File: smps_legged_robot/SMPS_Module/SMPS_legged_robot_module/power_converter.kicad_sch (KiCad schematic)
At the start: 80 parts, among them IC1 LTC3889EUKG#PBF, IC2 LTC3889EUKG#PBF, Q1 NMOS, Q10 NMOS, Q2 NMOS, Q3 NMOS, Q4 NMOS, Q5 PNP, Q6 PNP, Q7 NMOS, Q8 NMOS, Q9 NMOS

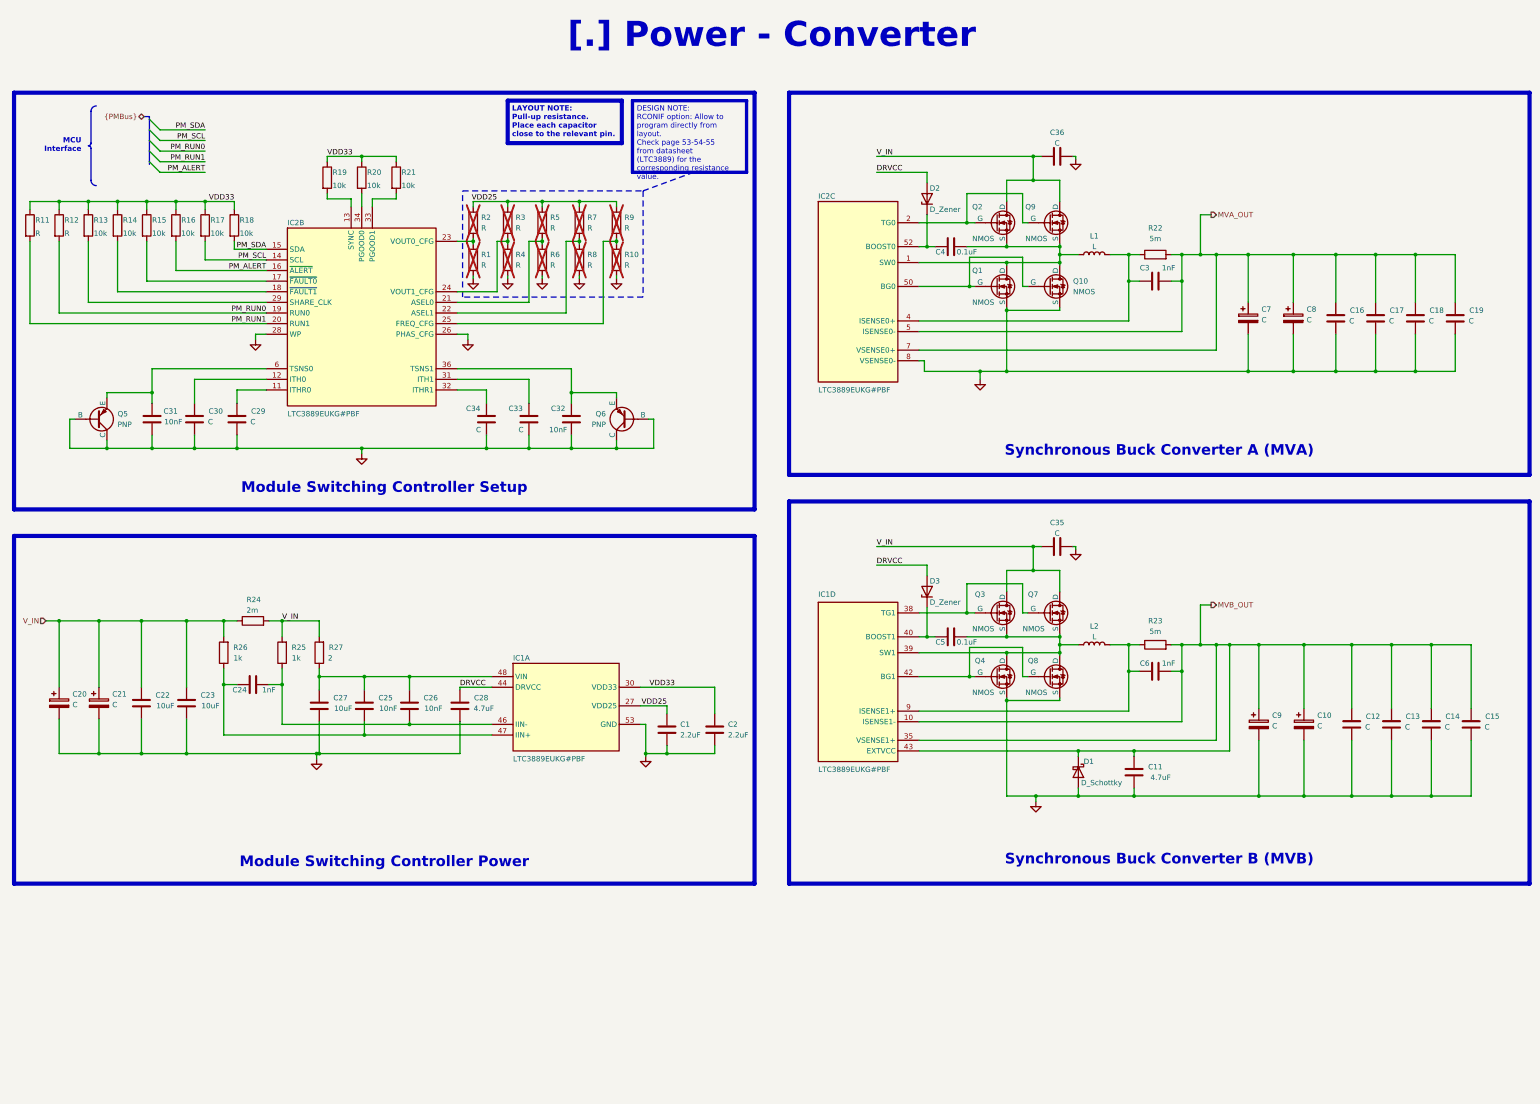
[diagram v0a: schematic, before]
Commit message: Buck module finished pending review
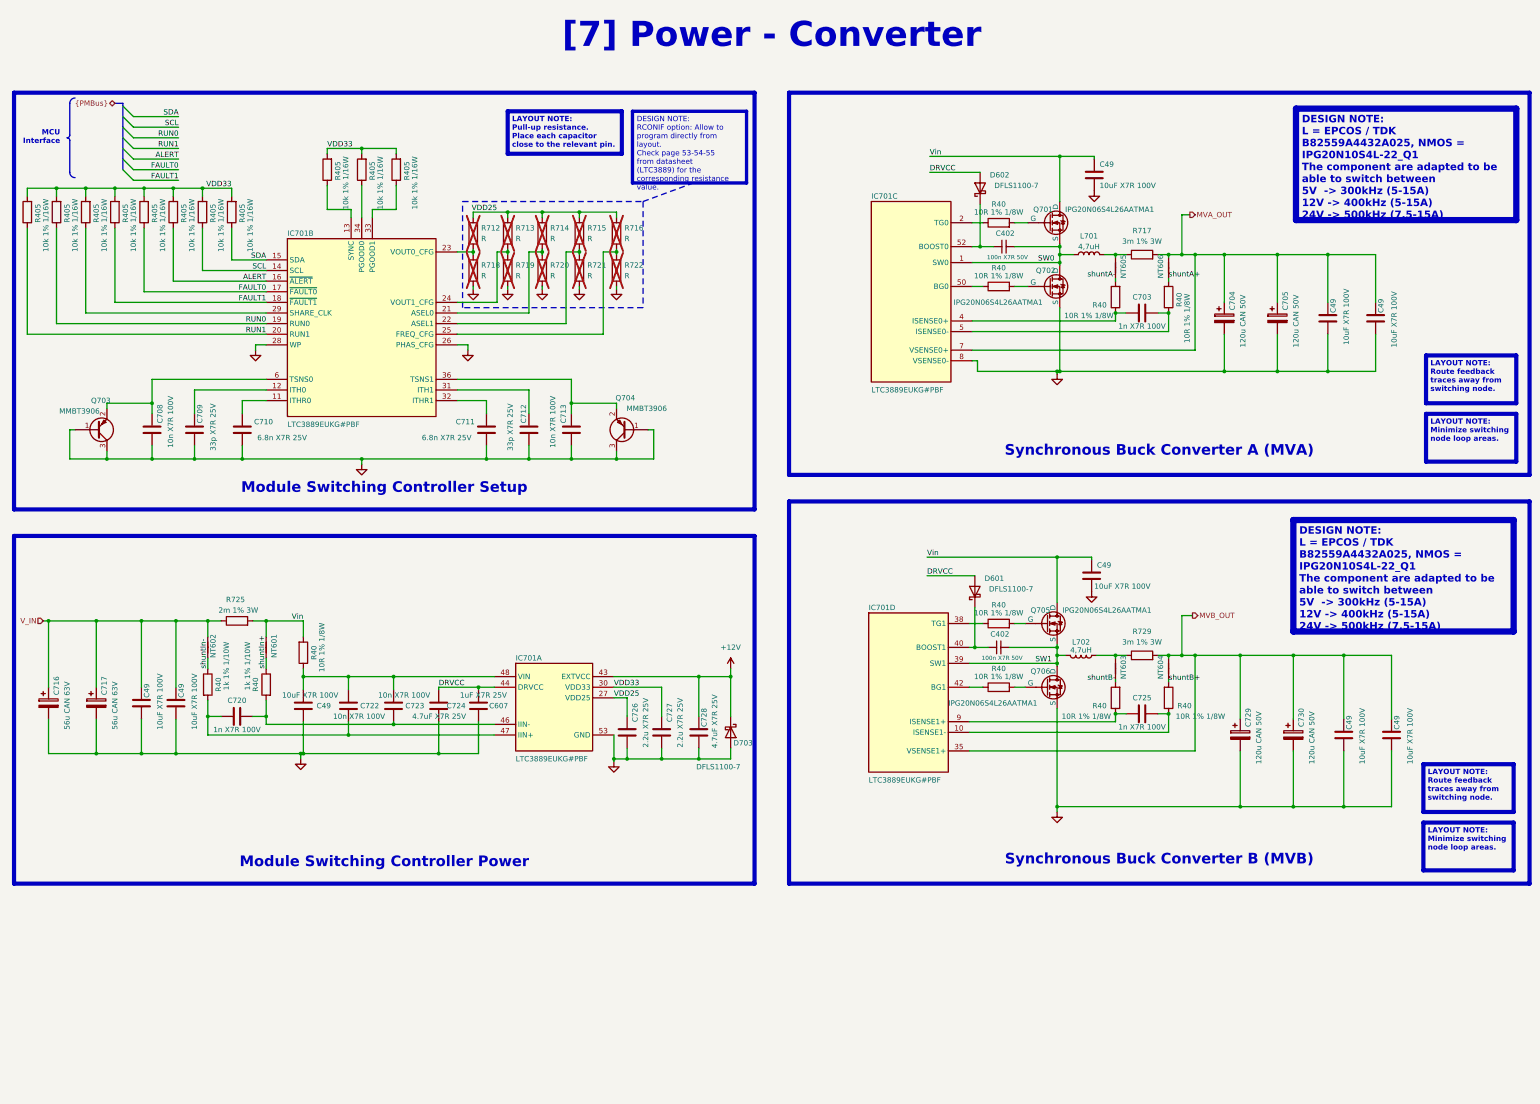
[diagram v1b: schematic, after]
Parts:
- removed C1, C2: 2.2uF, symbol Device:C
- removed C10, C21, C7, C8, C9: C, symbol Device:C_Polarized
- removed C11, C28: 4.7uF, symbol Device:C
- removed C12, C13, C14, C15, C16, C17, C18, C19, C30, C33, C34, C35, C36: C, symbol Device:C
- removed C22, C23, C27: 10uF, symbol Device:C
- removed C24, C3: 1nF, symbol Device:C
- removed C31, C32: 10nF, symbol Device:C
- removed C4, C5: 0.1uF, symbol Device:C
- removed D1: D_Schottky, symbol Device:D_Schottky
- removed D2, D3: D_Zener, symbol Device:D_Zener
- removed Q10, Q2, Q7, Q8, Q9: NMOS, symbol Simulation_SPICE:NMOS
- removed Q5, Q6: PNP, symbol Simulation_SPICE:PNP
- removed R11, R12: R, symbol Device:R
- removed R13, R14, R15, R16, R17, R18, R19, R20, R21: 10k, symbol Device:R
- removed R23: 5m, symbol Device:R
- removed R24: 2m, symbol Device:R
- removed R25, R26: 1k, symbol Device:R
- removed R27: 2, symbol Device:R
- added C402 (x2): 100n X7R 50V, 0_capacitor_smd:C_0402_1005_DensityHigh, symbol Device:C_Small
- added C49 (x9): 10uF X7R 100V, 0_capacitor_smd:C_1210_3225_DensityHigh, symbol Device:C
- added C607: 1uF X7R 25V, 0_capacitor_smd:C_0603_1608_DensityHigh, symbol Device:C
- added C703, C720: 1n X7R 100V, 0_capacitor_smd:C_0402_1005_DensityHigh, symbol Device:C
- added C704, C705, C729, C730: 120u CAN 50V, 0_capacitor_smd:Hybrid_G_VP, symbol Device:C_Polarized
- added C708, C713: 10n X7R 100V, 0_capacitor_smd:C_0402_1005_DensityHigh, symbol Device:C
- added C709, C712: 33p X7R 25V, 0_capacitor_smd:C_0402_1005_DensityHigh, symbol Device:C
- added C711: 6.8n X7R 25V, 0_capacitor_smd:C_0402_1005_DensityHigh, symbol Device:C
- added C717: 56u CAN 63V, 0_capacitor_smd:Hybrid_G_VP, symbol Device:C_Polarized
- added C724, C728: 4.7uF X7R 25V, 0_capacitor_smd:C_1210_3225_DensityHigh, symbol Device:C
- added C726, C727: 2.2u X7R 25V, 0_capacitor_smd:C_0805_2012_DensityHigh, symbol Device:C
- added D601, D602, D703: DFLS1100-7, 0_diode_smd:Diodes_Inc.-PowerDI123-03_2017-0-MFG, symbol Device:D_Schottky
- added NT601, NT602, NT603, NT604, NT605, NT606: NetTie_2, 0_net_tie:NetTie-2_SMD_Pad0.2mm, symbol Device:NetTie_2
- added Q701: IPG20N06S4L26AATMA1, 0_transistor_fet:Infineon-IPG20N06S4L-26A-Manufacturer_Recommended, symbol Simulation_SPICE:NMOS
- added Q703, Q704: MMBT3906, Package_TO_SOT_SMD:SOT-23, symbol Transistor_BJT:MMBT3906
- added R40 (x2): 1k 1% 1/10W, 0_resistor_smd:R_0603_1608_DensityHigh, symbol Device:R
- added R40 (x9): 10R 1% 1/8W, 0_resistor_smd:R_0402_1005_DensityHigh, symbol Device:R
- added R405 (x11): 10k 1% 1/16W, 0_resistor_smd:R_0402_1005_DensityHigh, symbol Device:R
- added R725: 2m 1% 3W, Resistor_SMD:R_2512_6332Metric_Pad1.40x3.35mm_HandSolder, symbol Device:R
- added R729: 3m 1% 3W, 0_resistor_smd:RESC6432X135N, symbol Device:R
- C710: renamed from C29; value C -> 6.8n X7R 25V; footprint (none) -> 0_capacitor_smd:C_0402_1005_DensityHigh
- C716: renamed from C20; value C -> 56u CAN 63V; footprint (none) -> 0_capacitor_smd:Hybrid_G_VP
- C722: renamed from C25; value 10nF -> 10n X7R 100V; footprint (none) -> 0_capacitor_smd:C_0402_1005_DensityHigh
- C723: renamed from C26; value 10nF -> 10n X7R 100V; footprint (none) -> 0_capacitor_smd:C_0402_1005_DensityHigh
- C725: renamed from C6; value 1nF -> 1n X7R 100V; footprint (none) -> 0_capacitor_smd:C_0402_1005_DensityHigh
- IC701: renamed from IC1; footprint QFN50P700X800X80-53N-D -> 0_switching_regulator:QFN50P700X800X80-53N-D
- IC701: renamed from IC2; footprint QFN50P700X800X80-53N-D -> 0_switching_regulator:QFN50P700X800X80-53N-D
- L701: renamed from L1; value L -> 4,7uH; footprint (none) -> 0_capacitor_smd:PQ2617BHA4R7K
- L702: renamed from L2; value L -> 4,7uH; footprint (none) -> 0_capacitor_smd:PQ2617BHA4R7K
- Q702: renamed from Q1; value NMOS -> IPG20N06S4L26AATMA1; footprint (none) -> 0_transistor_fet:Infineon-IPG20N06S4L-26A-Manufacturer_Recommended
- Q705: renamed from Q3; value NMOS -> IPG20N06S4L26AATMA1; footprint (none) -> 0_transistor_fet:Infineon-IPG20N06S4L-26A-Manufacturer_Recommended
- Q706: renamed from Q4; value NMOS -> IPG20N06S4L26AATMA1; footprint (none) -> 0_transistor_fet:Infineon-IPG20N06S4L-26A-Manufacturer_Recommended
- R712: renamed from R2; footprint (none) -> 0_resistor_smd:R_0402_1005_DensityHigh
- R713: renamed from R3; footprint (none) -> 0_resistor_smd:R_0402_1005_DensityHigh
- R714: renamed from R5; footprint (none) -> 0_resistor_smd:R_0402_1005_DensityHigh
- R715: renamed from R7; footprint (none) -> 0_resistor_smd:R_0402_1005_DensityHigh
- R716: renamed from R9; footprint (none) -> 0_resistor_smd:R_0402_1005_DensityHigh
- R717: renamed from R22; value 5m -> 3m 1% 3W; footprint (none) -> 0_resistor_smd:RESC6432X135N
- R718: renamed from R1; footprint (none) -> 0_resistor_smd:R_0402_1005_DensityHigh
- R719: renamed from R4; footprint (none) -> 0_resistor_smd:R_0402_1005_DensityHigh
- R720: renamed from R6; footprint (none) -> 0_resistor_smd:R_0402_1005_DensityHigh
- R721: renamed from R8; footprint (none) -> 0_resistor_smd:R_0402_1005_DensityHigh
- R722: renamed from R10; footprint (none) -> 0_resistor_smd:R_0402_1005_DensityHigh
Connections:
- net DRVCC: now also C607.2, C724.2, D601.2 (A), D602.2 (A)
- net GND: now also C49.2, C49.2, C49.2, C49.2, C49.2, C49.2, C49.2, C49.2, C49.2, C607.1, C704.2, C705.2, C708.1, C709.1, C711.1, C712.1, C713.1, C717.2, C724.1, C726.1, C727.1, C728.1, C729.2, C730.2, D703.2 (A), Q703.1 (B), Q703.3 (C), Q704.1 (B), Q704.3 (C)
- net MVA_OUT: now also C49.1, C49.1, C704.1, C705.1, NT606.1; no longer IC701.5 (ISENSE0-)
- net MVB_OUT: now also C49.1, C49.1, C729.1, C730.1, NT604.1, R729.2; no longer C725.2, IC701.10 (ISENSE1-), IC701.43 (EXTVCC)
- net VDD25: now also C726.2
- net VDD33: now also C727.2, R405.2, R405.2, R405.2, R405.2, R405.2, R405.2, R405.2, R405.2, R405.2, R405.2, R405.2
- net V_IN: now also C49.1, C49.1, C717.1, NT602.1, R725.1; no longer Q705.1 (D)
- net at Q705.2 (G): now also R40.2; no longer IC701.38 (TG1)
- net SW1: now reaches IC701.39 (SW1), Q705.3 (S), Q706.1 (D)
- net SW1: now also L702.2, C402.2; no longer L702.1
- net SW0: now reaches IC701.1 (SW0), L701.1, Q702.1 (D)
- net SW0: now also C402.2, Q701.3 (S)
- net at Q702.2 (G): now also R40.2; no longer IC701.50 (BG0)
- net at IC701.31 (ITH1): now also C712.2
- net at IC701.52 (BOOST0): now also C402.1, D602.1 (K)
- net at C722.2, C723.2, IC701.48 (VIN): now also C49.1, R40.1
- net at IC701.6 (TSNS0): now also C708.2, Q703.2 (E)
- net at L701.2, R717.1: now also NT605.1; no longer IC701.4 (ISENSE0+)
- net at C723.1, IC701.46 (IIN-): now also C720.2, R40.2
- net at C722.1, IC701.47 (IIN+): now also C720.1, R40.2
- net at IC701.13 (SYNC): now also R405.1
- net at IC701.2 (TG0): now also R40.1
- net at IC701.33 (PGOOD1): now also R405.1
- net at IC701.29 (SHARE_CLK): now also R405.1
- net FAULT0: now reaches IC701.17 (~{FAULT0})
- net FAULT0: now also R405.1
- net at IC701.12 (ITH0): now also C709.2
- net FAULT1: now reaches IC701.18 (~{FAULT1})
- net FAULT1: now also R405.1
- net at IC701.32 (ITHR1): now also C711.2
- net at IC701.34 (PGOOD0): now also R405.1
- net at IC701.36 (TSNS1): now also C713.2, Q704.2 (E)
- net at C725.1, IC701.9 (ISENSE1+): now also R40.1; no longer L702.2
- net at IC701.40 (BOOST1): now also C402.1, D601.1 (K)
- net at IC701.42 (BG1): now also R40.1; no longer Q706.2 (G)
- net PM_ALERT renamed ALERT
- net ALERT: now also R405.1
- net PM_RUN0 renamed RUN0
- net RUN0: now also R405.1
- net PM_RUN1 renamed RUN1
- net RUN1: now also R405.1
- net PM_SCL renamed SCL
- net SCL: now also R405.1
- net PM_SDA renamed SDA
- net SDA: now also R405.1
- new net: Q701.2 (G), R40.2
- new net: C703.2, IC701.5 (ISENSE0-), R40.1
- new net: C725.2, IC701.10 (ISENSE1-), R40.1
- new net: IC701.38 (TG1), R40.1
- new net: L702.1, NT603.1, R729.1
- new net: Q706.2 (G), R40.2
- new net: C703.1, IC701.4 (ISENSE0+), R40.1
- new net: IC701.50 (BG0), R40.1
- new net +12V: C728.2, D703.1 (K), IC701.43 (EXTVCC)
- new net Vin: C49.1, C49.1, NT601.1, Q701.1 (D), Q705.1 (D), R40.2, R725.2
- new net shuntA+: NT606.2, R40.2
- new net shuntA-: NT605.2, R40.2
- new net shuntB+: NT604.2, R40.2
- new net shuntB-: NT603.2, R40.2
- new net shuntIn+: NT601.2, R40.1
- new net shuntIn-: NT602.2, R40.1
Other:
- moved on the sheet: C710, C716, C722, C723, C725, IC701B, IC701C, L701, L702, Q702, Q705, Q706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

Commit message: Correction module
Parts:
- removed C49 (x3): 10uF X7R 100V, 0_capacitor_smd:C_1210_3225_DensityHigh, symbol Device:C
- removed C716, C717: 56u CAN 63V, 0_capacitor_smd:Hybrid_G_VP, symbol Device:C_Polarized
- removed C727: 2.2u X7R 25V, 0_capacitor_smd:C_0805_2012_DensityHigh, symbol Device:C
- removed C728: 4.7uF X7R 25V, 0_capacitor_smd:C_1210_3225_DensityHigh, symbol Device:C
- removed R40 (x4): 10R 1% 1/8W, 0_resistor_smd:R_0402_1005_DensityHigh, symbol Device:R
- added C716: 2.2u X7R 25V, 0_capacitor_smd:C_0603_1608_DensityHigh, symbol Device:C
- added C717: 4.7u X5R 25V, 0_capacitor_smd:C_0402_1005_DensityHigh, symbol Device:C
- added C718: 10n X7R 100V, 0_capacitor_smd:C_0402_1005_DensityHigh, symbol Device:C
- added D701, D702: LED, symbol Device:LED
- added Q707, Q708: NMOS, symbol Simulation_SPICE:NMOS
- added R40 (x6): 2R 1% 1/8W, 0_resistor_smd:R_0402_1005_DensityHigh, symbol Device:R
- added R736, R737: R, symbol Device:R
- added TP409: 3V3LTC, 0_testpoint:TestPoint_Pad_D0.5mm_Back, symbol Connector:TestPoint
- added TP409: VIN_MOS, 0_testpoint:TestPoint_Pad_D0.5mm_Front, symbol Connector:TestPoint
- added TP409: VIN, 0_testpoint:TestPoint_Pad_D0.5mm_Front, symbol Connector:TestPoint
- added TP409: DRVCC, 0_testpoint:TestPoint_Pad_D0.5mm_Back, symbol Connector:TestPoint
- added TP409: MVB_OUT, 0_testpoint:TestPoint_Pad_D0.5mm_Front, symbol Connector:TestPoint
- added TP409: SW1_L, 0_testpoint:TestPoint_Pad_D0.5mm_Front, symbol Connector:TestPoint
- added TP409: SW0, 0_testpoint:TestPoint_Pad_D0.5mm_Front, symbol Connector:TestPoint
- added TP409: SW0_L, 0_testpoint:TestPoint_Pad_D0.5mm_Front, symbol Connector:TestPoint
- added TP409: MVA_OUT, 0_testpoint:TestPoint_Pad_D0.5mm_Front, symbol Connector:TestPoint
- added TP409: 2V5LTC, 0_testpoint:TestPoint_Pad_D0.5mm_Back, symbol Connector:TestPoint
- added TP409: SW1, 0_testpoint:TestPoint_Pad_D0.5mm_Front, symbol Connector:TestPoint
- C607: value 1uF X7R 25V -> 1u X7R 25V
- C724: value 4.7uF X7R 25V -> 4.7u X5R 25V; footprint 0_capacitor_smd:C_1210_3225_DensityHigh -> 0_capacitor_smd:C_0402_1005_DensityHigh
- C726: footprint 0_capacitor_smd:C_0805_2012_DensityHigh -> 0_capacitor_smd:C_0603_1608_DensityHigh
- Q703, Q704: value MMBT3906 -> PMBT3906,215
- R40: value 10R 1% 1/8W -> 2R 1% 1/8W
- R405: value 10k 1% 1/16W -> 5k 1% 1/16W
- R712, R713, R714, R715, R718, R719, R720, R721: now left out of the parts list
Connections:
- net +12V: now also C717.2, R736.1, R737.1
- net DRVCC: now also TP409.1
- net GND: now also C716.1, C717.1, C718.1, Q707.3 (S), Q708.3 (S)
- net MVA_OUT: now also TP409.1
- net MVB_OUT: now also TP409.1
- net SW0: now also TP409.1
- net SW1: now also TP409.1
- net at Q705.2 (G): now also R40.1
- net at Q701.2 (G): now also R40.1
- net SW0_L: now reaches L701.2, NT605.1, R717.1
- net SW0_L: now also TP409.1
- net at IC701.2 (TG0): now also R40.2
- net VIN: now reaches C722.2, C723.2, IC701.48 (VIN), R40.1
- net VIN: now also C718.2, TP409.1
- net PGOOD1: now reaches IC701.33 (PGOOD1), R405.1
- net PGOOD1: now also Q708.2 (G)
- net at D601.1 (K), IC701.40 (BOOST1): now also R40.2; no longer C402.1
- net at Q702.2 (G): now also R40.1
- net at IC701.38 (TG1): now also R40.2
- net SW1_L: now reaches L702.1, NT603.1, R729.1
- net SW1_L: now also TP409.1
- net SHARE_CLK: now reaches IC701.29 (SHARE_CLK), R405.1
- net at IC701.42 (BG1): now also R40.2
- net at Q706.2 (G): now also R40.1
- net PGOOD0: now reaches IC701.34 (PGOOD0), R405.1
- net PGOOD0: now also Q707.2 (G)
- net SYNC: now reaches IC701.13 (SYNC), R405.1
- net at IC701.50 (BG0): now also R40.2
- net at D602.1 (K), IC701.52 (BOOST0): now also R40.2; no longer C402.1
- net ALERT renamed ~{ALERT}
- net FAULT0 renamed ~{FAULT0}
- net FAULT1 renamed ~{FAULT1}
- net VDD25 renamed +2V5LTC
- net +2V5LTC: now also TP409.1
- net VDD33 renamed +3.3VLTC
- net +3.3VLTC: now also C716.2, TP409.1
- net V_IN renamed +VBAT_FILTERED
- net Vin renamed VIN_MOS
- net VIN_MOS: now also TP409.1
- new net: D701.1 (K), Q707.1 (D)
- new net: D701.2 (A), R736.2
- new net: C402.1, R40.1 (x2)
- new net: D702.2 (A), R737.2
- new net: D702.1 (K), Q708.1 (D)
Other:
- moved on the sheet: C402, C49, C607, C704, C705, C708, C709, C710, C711, C712, C713, C720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
